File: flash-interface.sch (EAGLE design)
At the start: 3 parts, among them U1 W25N01GVZEIG_TR

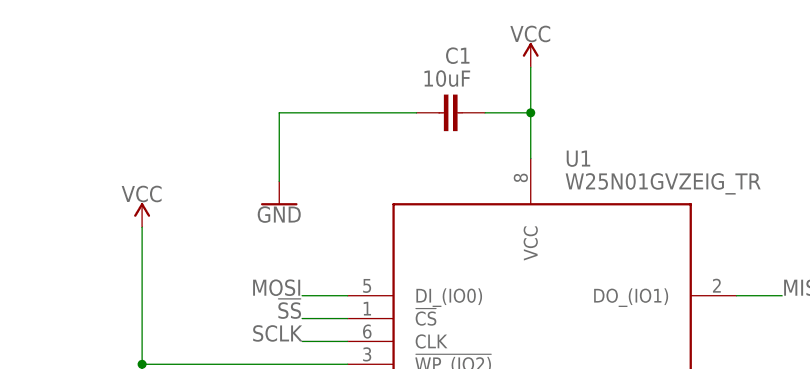
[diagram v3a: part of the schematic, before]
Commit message: Replaced 0603 cap with 0805, fully routed board
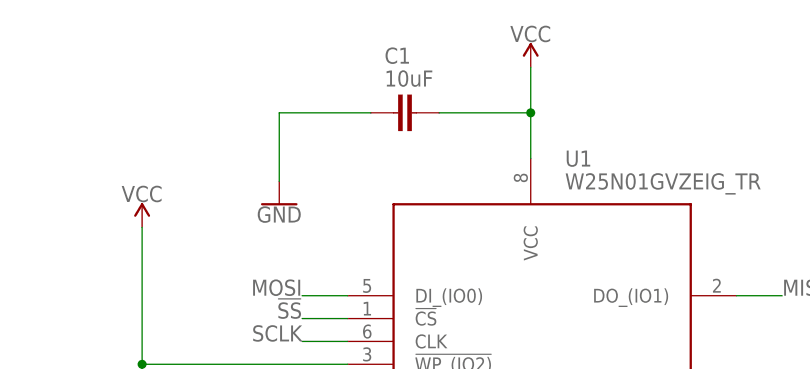
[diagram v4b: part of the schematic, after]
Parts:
- C1: device SparkFun-Capacitors:10UF-0603-6.3V-20% -> SparkFun-Capacitors:10UF-0805-10V-10%
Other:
- moved on the sheet: C1
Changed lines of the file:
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@@
 <part name="SUPPLY2" library="SparkFun-PowerSymbols" library_urn="urn:adsk.eagle:library:530" deviceset="VCC" device=""/>
 <part name="GND2" library="SparkFun-PowerSymbols" library_urn="urn:adsk.eagle:library:530" deviceset="GND" device=""/>
-<part name="C1" library="SparkFun-Capacitors" library_urn="urn:adsk.eagle:library:510" deviceset="10UF" device="-0603-6.3V-20%" package3d_urn="urn:adsk.eagle:package:37414/1" value="10uF"/>
 <part name="GND7" library="SparkFun-PowerSymbols" library_urn="urn:adsk.eagle:library:530" deviceset="GND" device=""/>
 <part name="SUPPLY5" library="SparkFun-PowerSymbols" library_urn="urn:adsk.eagle:library:530" deviceset="VCC" device=""/>
@@
 <part name="GND3" library="SparkFun-PowerSymbols" library_urn="urn:adsk.eagle:library:530" deviceset="GND" device=""/>
 <part name="SUPPLY1" library="SparkFun-PowerSymbols" library_urn="urn:adsk.eagle:library:530" deviceset="VCC" device=""/>
+<part name="C1" library="SparkFun-Capacitors" library_urn="urn:adsk.eagle:library:510" deviceset="10UF" device="-0805-10V-10%" package3d_urn="urn:adsk.eagle:package:37429/1" value="10uF"/>
 </parts>
 <sheets>
@@
 <instance part="GND2" gate="1" x="177.8" y="27.94" smashed="yes">
 <attribute name="VALUE" x="177.8" y="27.686" size="1.778" layer="96" align="top-center"/>
-</instance>
-<instance part="C1" gate="G$1" x="167.64" y="81.28" smashed="yes" rot="MR90">
-<attribute name="NAME" x="171.196" y="86.741" size="1.778" layer="95" font="vector" rot="MR0"/>
-<attribute name="VALUE" x="171.196" y="84.201" size="1.778" layer="96" font="vector" rot="MR0"/>
 </instance>
 <instance part="GND7" gate="1" x="149.86" y="71.12" smashed="yes">
@@
 <attribute name="VALUE" x="78.74" y="68.834" size="1.778" layer="96" align="bottom-center"/>
 </instance>
+<instance part="C1" gate="G$1" x="162.56" y="81.28" smashed="yes" rot="R270">
+<attribute name="NAME" x="161.544" y="86.741" size="1.778" layer="95" font="vector"/>
+<attribute name="VALUE" x="161.544" y="84.201" size="1.778" layer="96" font="vector"/>
+</instance>
 </instances>
 <busses>
@@
 <net name="GND" class="0">
 <segment>
-<pinref part="C1" gate="G$1" pin="2"/>
-<wire x1="165.1" y1="81.28" x2="149.86" y2="81.28" width="0.1524" layer="91"/>
+<wire x1="160.02" y1="81.28" x2="149.86" y2="81.28" width="0.1524" layer="91"/>
 <pinref part="GND7" gate="1" pin="GND"/>
 <wire x1="149.86" y1="81.28" x2="149.86" y2="73.66" width="0.1524" layer="91"/>
+<pinref part="C1" gate="G$1" pin="2"/>
 </segment>
 <segment>
@@
 <net name="VCC" class="0">
 <segment>
-<pinref part="C1" gate="G$1" pin="1"/>
-<wire x1="172.72" y1="81.28" x2="177.8" y2="81.28" width="0.1524" layer="91"/>
+<wire x1="167.64" y1="81.28" x2="177.8" y2="81.28" width="0.1524" layer="91"/>
 <pinref part="U1" gate="G$1" pin="VCC"/>
 <wire x1="177.8" y1="81.28" x2="177.8" y2="76.2" width="0.1524" layer="91"/>
@@
 <wire x1="177.8" y1="86.36" x2="177.8" y2="81.28" width="0.1524" layer="91"/>
 <junction x="177.8" y="81.28"/>
+<pinref part="C1" gate="G$1" pin="1"/>
 </segment>
 <segment>
